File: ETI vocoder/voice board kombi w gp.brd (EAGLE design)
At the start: 160 x 60.3 mm, 174 parts, among them IC1 TL072P, IC1. TL072P, IC2 TL072P, IC2. TL072P, IC3 TL081P, IC3. TL081P, IC4 TL081P, IC4. TL081P, IC5 TL072P, IC6 LM13600AN, IC7 TL072P, IC7. TL072P, P1 C-OR-R050_075-025X100, P1. C-OR-R050_075-025X100, P10 C-OR-R050_075-025X100, P10. C-OR-R050_075-025X100, P11 C-OR-R050_075-025X100, P11. C-OR-R050_075-025X100, P12 C-OR-R050_075-025X100, P12. C-OR-R050_075-025X100, P13 C-OR-R050_075-025X100, P13. C-OR-R050_075-025X100, P14 C-OR-R050_075-025X100, P14. C-OR-R050_075-025X100, P15 C-OR-R050_075-025X100, P15. C-OR-R050_075-025X100, P16 C-OR-R050_075-025X100, P16. C-OR-R050_075-025X100, P2 C-OR-R050_075-025X100, P2. C-OR-R050_075-025X100, P3 C-OR-R050_075-025X100, P3. C-OR-R050_075-025X100, P4 C-OR-R050_075-025X100, P4. C-OR-R050_075-025X100, P5 C-OR-R050_075-025X100, P5. C-OR-R050_075-025X100, P6 C-OR-R050_075-025X100, P6. C-OR-R050_075-025X100, P7 C-OR-R050_075-025X100, P7. C-OR-R050_075-025X100, P8 C-OR-R050_075-025X100, P8. C-OR-R050_075-025X100, P9 C-OR-R050_075-025X100, P9. C-OR-R050_075-025X100, Q1 BF244C, Q1. BF244C, Q2 BC212L, Q2. BC212L

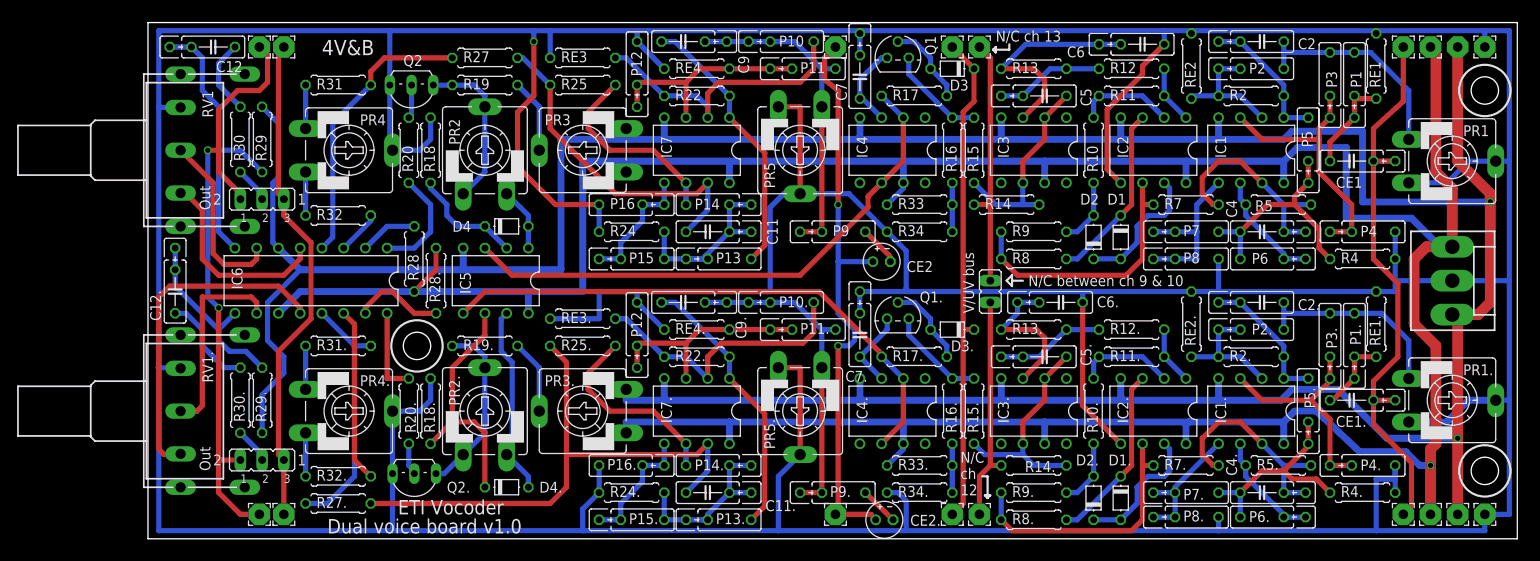
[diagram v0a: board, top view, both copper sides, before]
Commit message: Finished (I think) voice boards, added ground planes
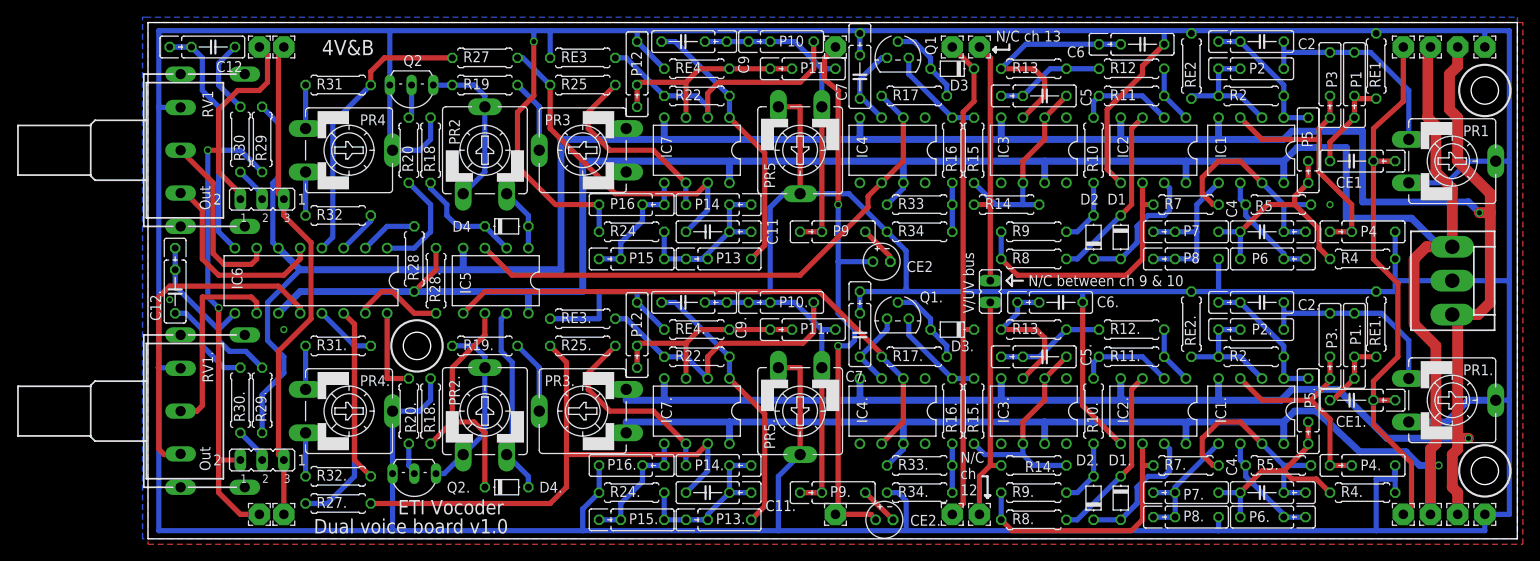
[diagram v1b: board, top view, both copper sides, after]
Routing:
- net -12V: track 398.1 -> 402.5 mm
- net +12V: track 366.7 -> 368.9 mm
- net GND: vias 1 -> 4
- added copper zone on layer 1, net GND
- added copper zone on layer 16, net GND
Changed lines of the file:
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@@
 <circle x="156.21" y="7.9375" radius="3" width="0.254" layer="25"/>
 <text x="20.32" y="56.515" size="1.778" layer="25" font="vector">4V&amp;B</text>
-<text x="20.955" y="0.635" size="1.6764" layer="25" font="vector">Dual voice board v1.0</text>
+<text x="19.3675" y="0.635" size="1.6764" layer="25" font="vector">Dual voice board v1.0</text>
 <text x="29.21" y="2.8575" size="1.6764" layer="25" font="vector">ETI Vocoder</text>
 <text x="95.25" y="55.5625" size="1.27" layer="26" font="vector" rot="MR270">Slew</text>
@@
 <wire x1="88.5825" y1="33.655" x2="88.5825" y2="29.21" width="0.6096" layer="16"/>
 <wire x1="88.5825" y1="29.21" x2="88.9" y2="28.8925" width="0.6096" layer="16"/>
+<polygon width="0.4064" layer="16">
+<vertex x="-0.3175" y="60.96"/>
+<vertex x="160.02" y="60.96"/>
+<vertex x="160.02" y="0"/>
+<vertex x="-0.635" y="0"/>
+<vertex x="-0.635" y="60.96"/>
+</polygon>
+<polygon width="0.4064" layer="1">
+<vertex x="0" y="60.325"/>
+<vertex x="0" y="-0.635"/>
+<vertex x="160.655" y="-0.635"/>
+<vertex x="160.655" y="60.325"/>
+</polygon>
+<via x="15.875" y="24.4475" extent="1-16" drill="0.5"/>
+<via x="138.1125" y="39.0525" extent="1-16" drill="0.5"/>
+<via x="2.54" y="27.94" extent="1-16" drill="0.5"/>
 </signal>
 <signal name="N$5">
@@
 <wire x1="44.45" y1="26.3525" x2="44.45" y2="28.8925" width="0.8128" layer="16"/>
 <wire x1="149.86" y1="57.4675" x2="149.86" y2="57.15" width="1.27" layer="1"/>
-<wire x1="149.86" y1="57.15" x2="150.495" y2="56.515" width="1.27" layer="1"/>
-<wire x1="150.495" y1="56.515" x2="150.495" y2="42.8625" width="1.27" layer="1"/>
+<wire x1="149.86" y1="57.15" x2="149.5425" y2="56.8325" width="1.27" layer="1"/>
+<wire x1="149.5425" y1="56.8325" x2="149.5425" y2="49.2125" width="1.27" layer="1"/>
+<wire x1="149.5425" y1="49.2125" x2="150.495" y2="48.26" width="1.27" layer="1"/>
+<wire x1="150.495" y1="48.26" x2="150.495" y2="42.8625" width="1.27" layer="1"/>
 <wire x1="150.495" y1="42.8625" x2="152.4" y2="40.9575" width="1.27" layer="1"/>
 <wire x1="152.4" y1="40.9575" x2="152.4" y2="34.1225" width="1.27" layer="1"/>
@@
 <wire x1="141.605" y1="10.16" x2="147.0025" y2="10.16" width="0.8128" layer="16"/>
 <wire x1="147.0025" y1="10.16" x2="148.59" y2="8.5725" width="0.8128" layer="16"/>
-<wire x1="148.59" y1="8.5725" x2="149.86" y2="8.5725" width="0.8128" layer="16"/>
-<via x="149.86" y="8.5725" extent="1-16" drill="0.6"/>
+<wire x1="148.59" y1="8.5725" x2="150.8125" y2="8.5725" width="0.8128" layer="16"/>
+<via x="150.8125" y="8.5725" extent="1-16" drill="0.6"/>
+<wire x1="150.8125" y1="8.5725" x2="149.86" y2="8.5725" width="0.8128" layer="1"/>
 <wire x1="149.86" y1="8.5725" x2="149.86" y2="10.4775" width="0.8128" layer="1"/>
 <wire x1="88.265" y1="11.1125" x2="88.265" y2="13.6525" width="0.8128" layer="16"/>
@@
 <contactref element="PAD13" pad="1"/>
 <contactref element="PAD14" pad="1"/>
-<wire x1="153.035" y1="57.4675" x2="153.035" y2="44.1325" width="1.27" layer="1"/>
+<wire x1="153.035" y1="57.4675" x2="153.035" y2="55.245" width="1.27" layer="1"/>
+<wire x1="153.035" y1="55.245" x2="152.0825" y2="54.2925" width="1.27" layer="1"/>
+<wire x1="152.0825" y1="54.2925" x2="152.0825" y2="50.165" width="1.27" layer="1"/>
+<wire x1="152.0825" y1="50.165" x2="153.035" y2="49.2125" width="1.27" layer="1"/>
+<wire x1="153.035" y1="49.2125" x2="153.035" y2="44.1325" width="1.27" layer="1"/>
 <wire x1="15.24" y1="33.9725" x2="17.78" y2="31.4325" width="0.8128" layer="16"/>
 <wire x1="17.78" y1="31.4325" x2="36.83" y2="31.4325" width="0.8128" layer="16"/>
@@
 <wire x1="55.88" y1="47.9425" x2="55.88" y2="46.6725" width="0.8128" layer="16"/>
 <wire x1="36.83" y1="33.9725" x2="36.83" y2="31.4325" width="0.8128" layer="16"/>
-<wire x1="153.035" y1="2.8575" x2="153.035" y2="11.7475" width="1.27" layer="1"/>
+<wire x1="153.035" y1="2.8575" x2="153.035" y2="5.3975" width="1.27" layer="1"/>
+<wire x1="153.035" y1="5.3975" x2="152.4" y2="6.0325" width="1.27" layer="1"/>
+<wire x1="152.4" y1="6.0325" x2="152.4" y2="9.8425" width="1.27" layer="1"/>
+<wire x1="152.4" y1="9.8425" x2="153.035" y2="10.4775" width="1.27" layer="1"/>
+<wire x1="153.035" y1="10.4775" x2="153.035" y2="11.7475" width="1.27" layer="1"/>
+<wire x1="154.305" y1="11.7475" x2="153.035" y2="11.7475" width="1.27" layer="1"/>
 <wire x1="153.035" y1="11.7475" x2="153.035" y2="26.3525" width="1.27" layer="1"/>
 <wire x1="156.845" y1="40.3225" x2="153.035" y2="44.1325" width="1.27" layer="1"/>
@@
 <wire x1="133.6675" y1="17.4625" x2="139.065" y2="17.4625" width="0.8128" layer="16"/>
 <wire x1="139.065" y1="17.4625" x2="144.78" y2="11.7475" width="0.8128" layer="16"/>
-<wire x1="144.78" y1="11.7475" x2="153.035" y2="11.7475" width="0.8128" layer="16"/>
+<wire x1="144.78" y1="11.7475" x2="154.305" y2="11.7475" width="0.8128" layer="16"/>
 <wire x1="132.3975" y1="16.1925" x2="125.095" y2="16.1925" width="0.8128" layer="16"/>
 <wire x1="125.095" y1="16.1925" x2="113.9825" y2="16.1925" width="0.8128" layer="16"/>
@@
 <wire x1="99.695" y1="18.7325" x2="99.695" y2="16.1925" width="0.8128" layer="16"/>
 <wire x1="141.9225" y1="47.625" x2="141.9225" y2="39.37" width="0.8128" layer="16"/>
-<wire x1="141.9225" y1="39.37" x2="156.845" y2="39.37" width="0.8128" layer="16"/>
+<wire x1="141.9225" y1="39.37" x2="154.305" y2="39.37" width="0.8128" layer="16"/>
+<wire x1="154.305" y1="39.37" x2="155.575" y2="38.1" width="0.8128" layer="16"/>
 <wire x1="155.425" y1="26.2025" x2="156.845" y2="27.6225" width="1.27" layer="1"/>
-<wire x1="156.845" y1="27.6225" x2="156.845" y2="39.37" width="1.27" layer="1"/>
-<wire x1="156.845" y1="39.37" x2="156.845" y2="40.3225" width="1.27" layer="1"/>
+<wire x1="156.845" y1="27.6225" x2="156.845" y2="38.1" width="1.27" layer="1"/>
+<wire x1="155.575" y1="38.1" x2="156.845" y2="38.1" width="1.27" layer="1"/>
+<wire x1="156.845" y1="38.1" x2="156.845" y2="40.3225" width="1.27" layer="1"/>
 <wire x1="17.78" y1="31.4325" x2="13.97" y2="27.6225" width="0.6096" layer="16"/>
 <wire x1="13.97" y1="27.6225" x2="13.97" y2="23.1775" width="0.6096" layer="16"/>
@@
 <wire x1="152.55" y1="26.3525" x2="152.4" y2="26.2025" width="1.27" layer="1"/>
 <wire x1="152.4" y1="26.2025" x2="155.425" y2="26.2025" width="1.27" layer="1"/>
-<via x="156.845" y="39.37" extent="1-16" drill="0.6"/>
-<via x="153.035" y="11.7475" extent="1-16" drill="0.6"/>
+<via x="155.575" y="38.1" extent="1-16" drill="0.6"/>
+<via x="154.305" y="11.7475" extent="1-16" drill="0.6"/>
 <contactref element="IC1." pad="4"/>
 <contactref element="IC2." pad="4"/>

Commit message: Added logo and did some minor fixes
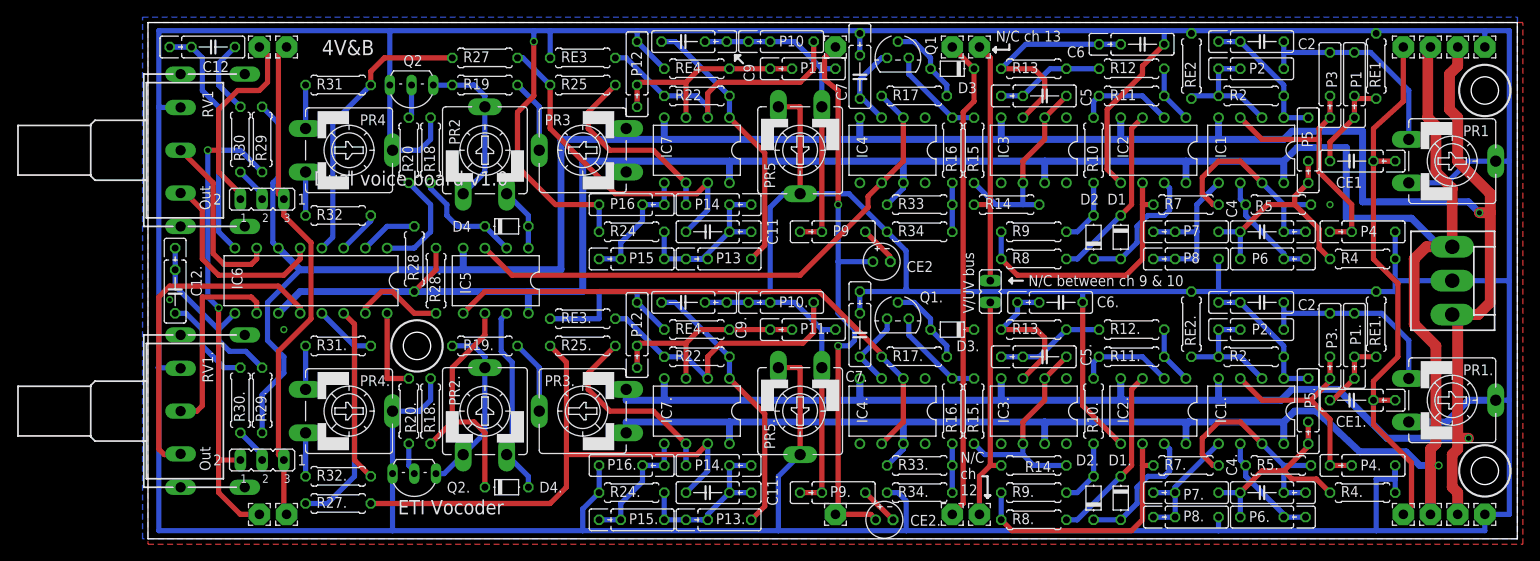
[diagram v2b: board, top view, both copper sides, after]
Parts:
- moved PAD1 0.32 mm to (16.2, 57.5)
- moved PAD2 0.32 mm to (16.2, 2.86)
- flipped PAD13 to the top

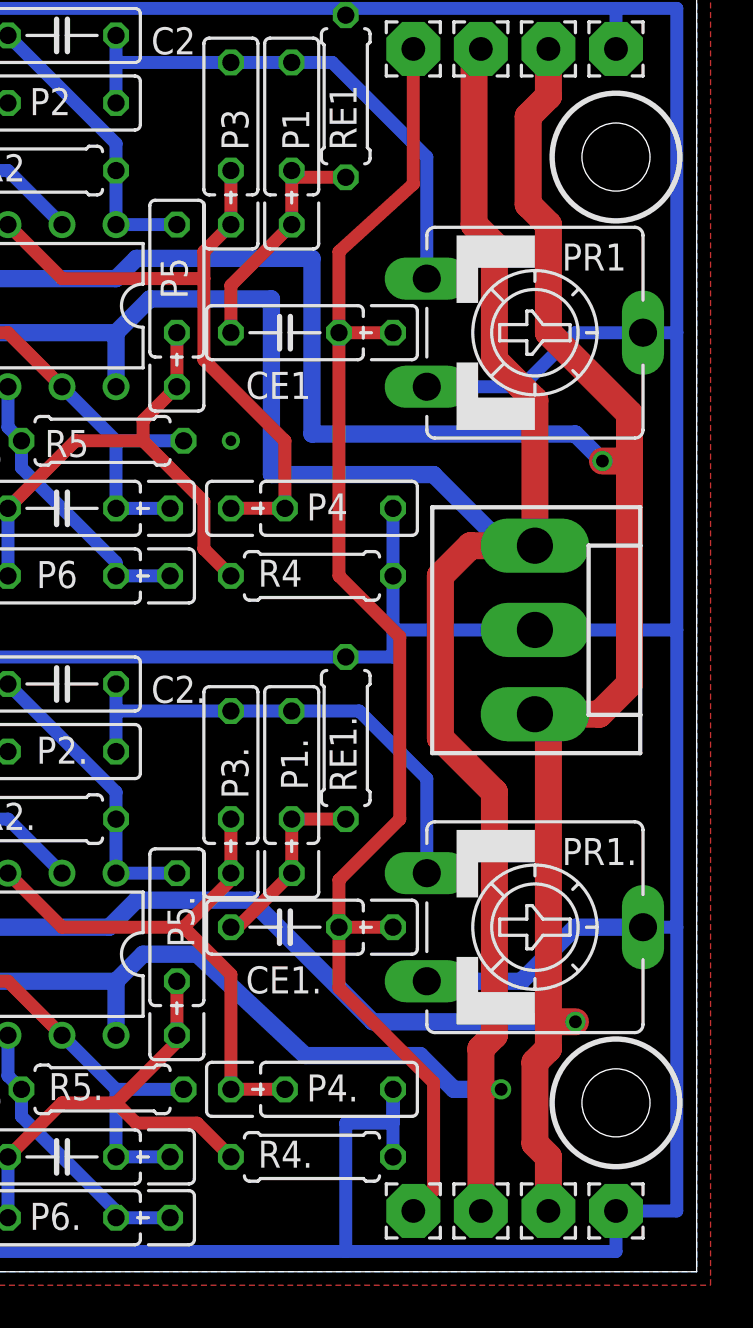
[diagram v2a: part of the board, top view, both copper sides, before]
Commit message: Send combined 4 to production. Fixed wrong CE1 footprint for voice cards. Removed outline from combined 4 that covered too much of a slot
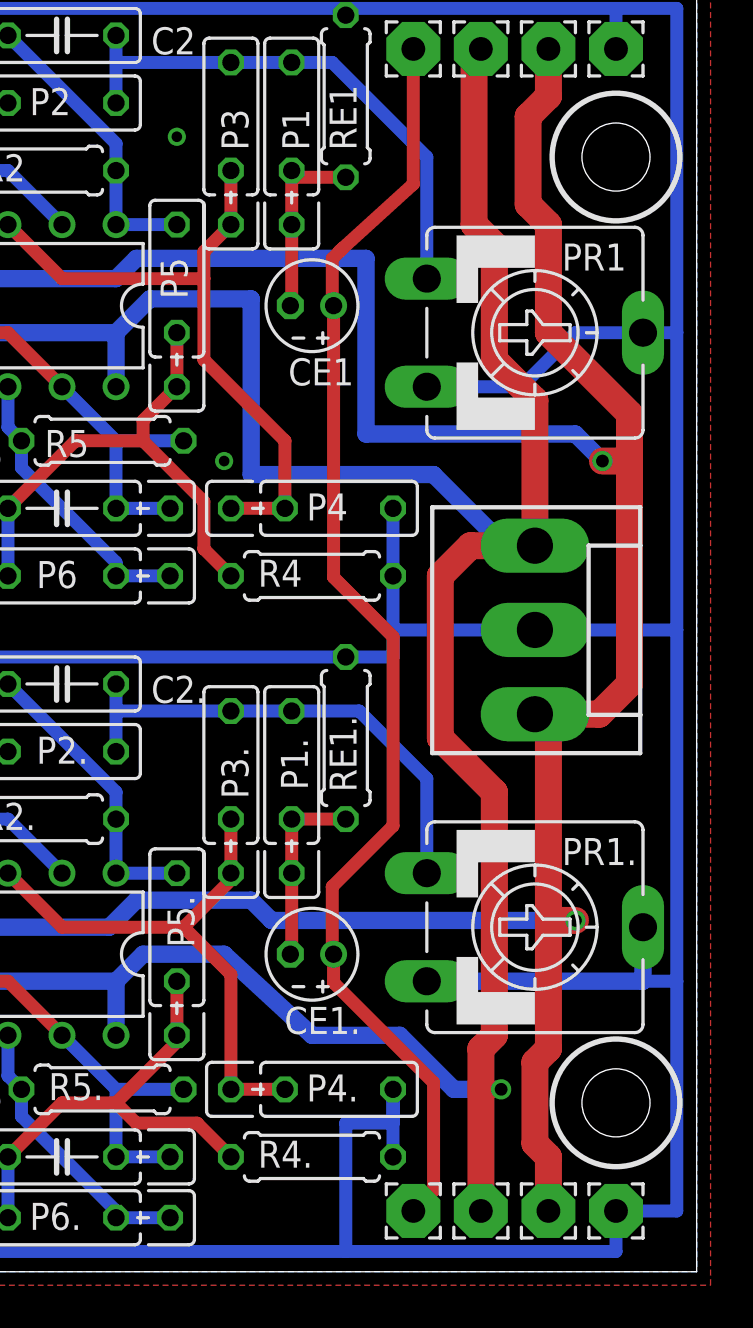
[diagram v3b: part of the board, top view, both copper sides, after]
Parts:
- CE1, CE1.: device joakim:C050_075-025X100J -> resistor:E2-4
- moved CE1 1.80 mm to (141.9, 45.4), turned to 180 degrees
- moved CE1. 1.80 mm to (141.9, 14.9), turned to 180 degrees
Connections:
- net N$43: now also CE1.-; no longer CE1.1
- net N$88: now also CE1..-; no longer CE1..1
- net SPEECH_IN: now also CE1.+, CE1..+; no longer CE1..2, CE1..3, CE1.2, CE1.3
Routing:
- net SPEECH_IN: track 65.8 -> 61.3 mm
- net N$43: track 11.7 -> 9.27 mm
- net -12V: track 402.5 -> 400.6 mm
- net GND: track 818.9 -> 817.3 mm, vias 4 -> 5
